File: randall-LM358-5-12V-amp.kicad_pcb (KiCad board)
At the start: 2 copper layers, 94 x 63.5 mm, 28 parts, among them J1 Power, Q1 TIP120, Q2 TIP120, U1 LM2674M-3.3, U2 LM358, U3 Z-Uno-Module

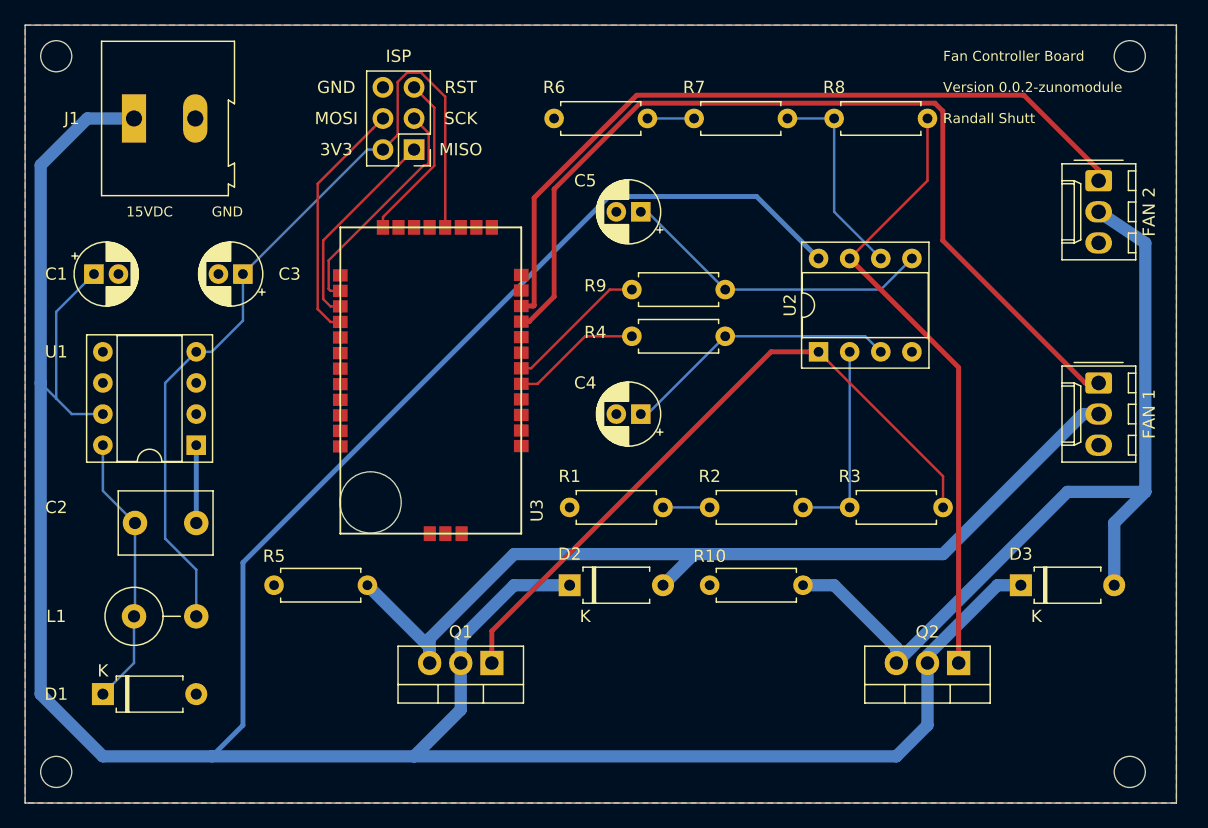
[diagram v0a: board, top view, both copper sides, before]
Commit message: Ok added an antenna and some keepouts and rerouted a trace or two:
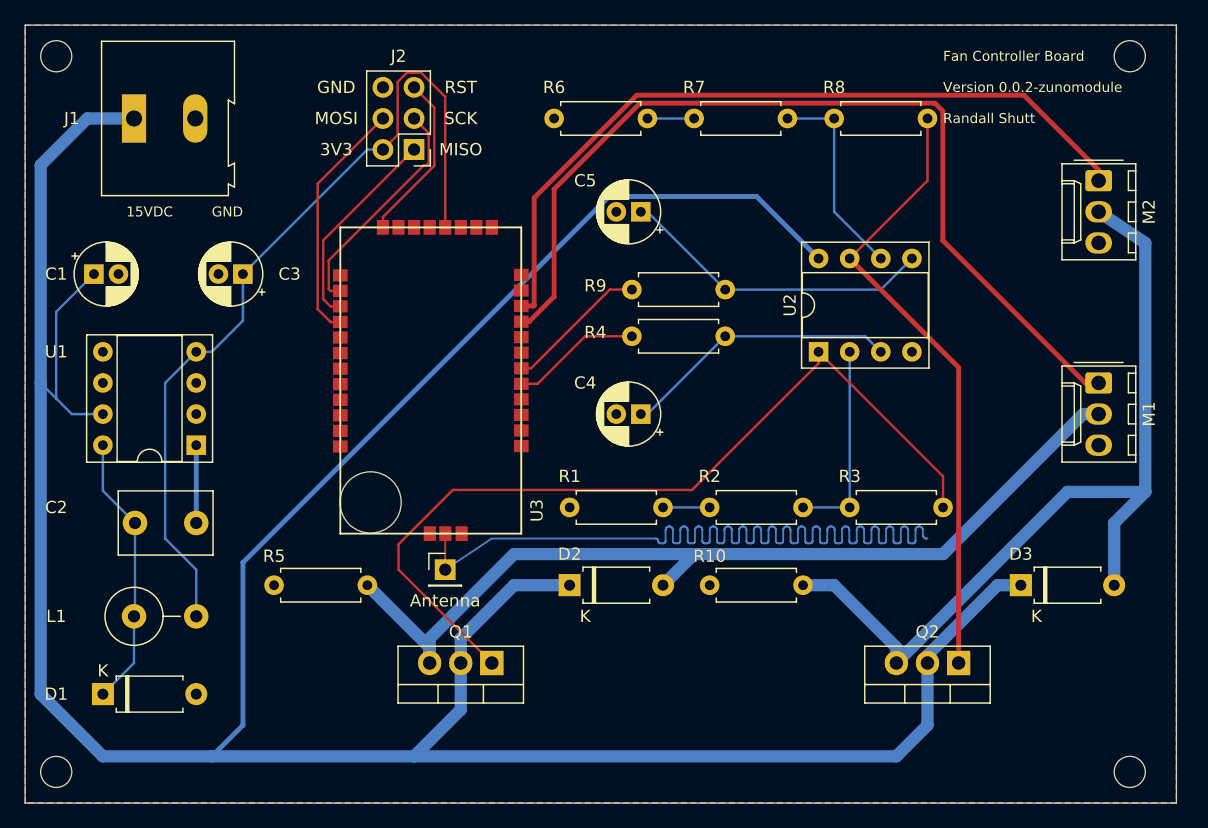
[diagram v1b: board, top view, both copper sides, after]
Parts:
- added Antenna: J3, Connector_PinHeader_2.54mm:PinHeader_1x01_P2.54mm_Vertical, F.Cu at (116.8, 104.1)
- J1: value Power -> Barrel_Jack
- M1: renamed from FAN 1
- M2: renamed from FAN 2
- renumbered ISP to J2
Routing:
- net Net-(J3-Pad1): track 0.00 -> 85.0 mm
- net Net-(Q1-Pad1): track 55.6 -> 71.1 mm

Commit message: Updating P/N
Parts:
- C1, C3: value 100uF -> 100uF OSCON-SEP
- C4, C5: value 100uF -> 100uF 25v
- D1: value D_Schottky -> 11DQ05TA
- J3: renamed from Antenna; value J3 -> Antenna Pin
- L1: value 68uH -> 68uH B78148E
- M1, M2: value Fan_3pin -> Molex 22282931
- U1: value LM2674M-3.3 -> LM2674N-3.3/NOPB
- U2: value LM358 -> LM358N/NOPB
